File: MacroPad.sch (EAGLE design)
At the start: 16 parts

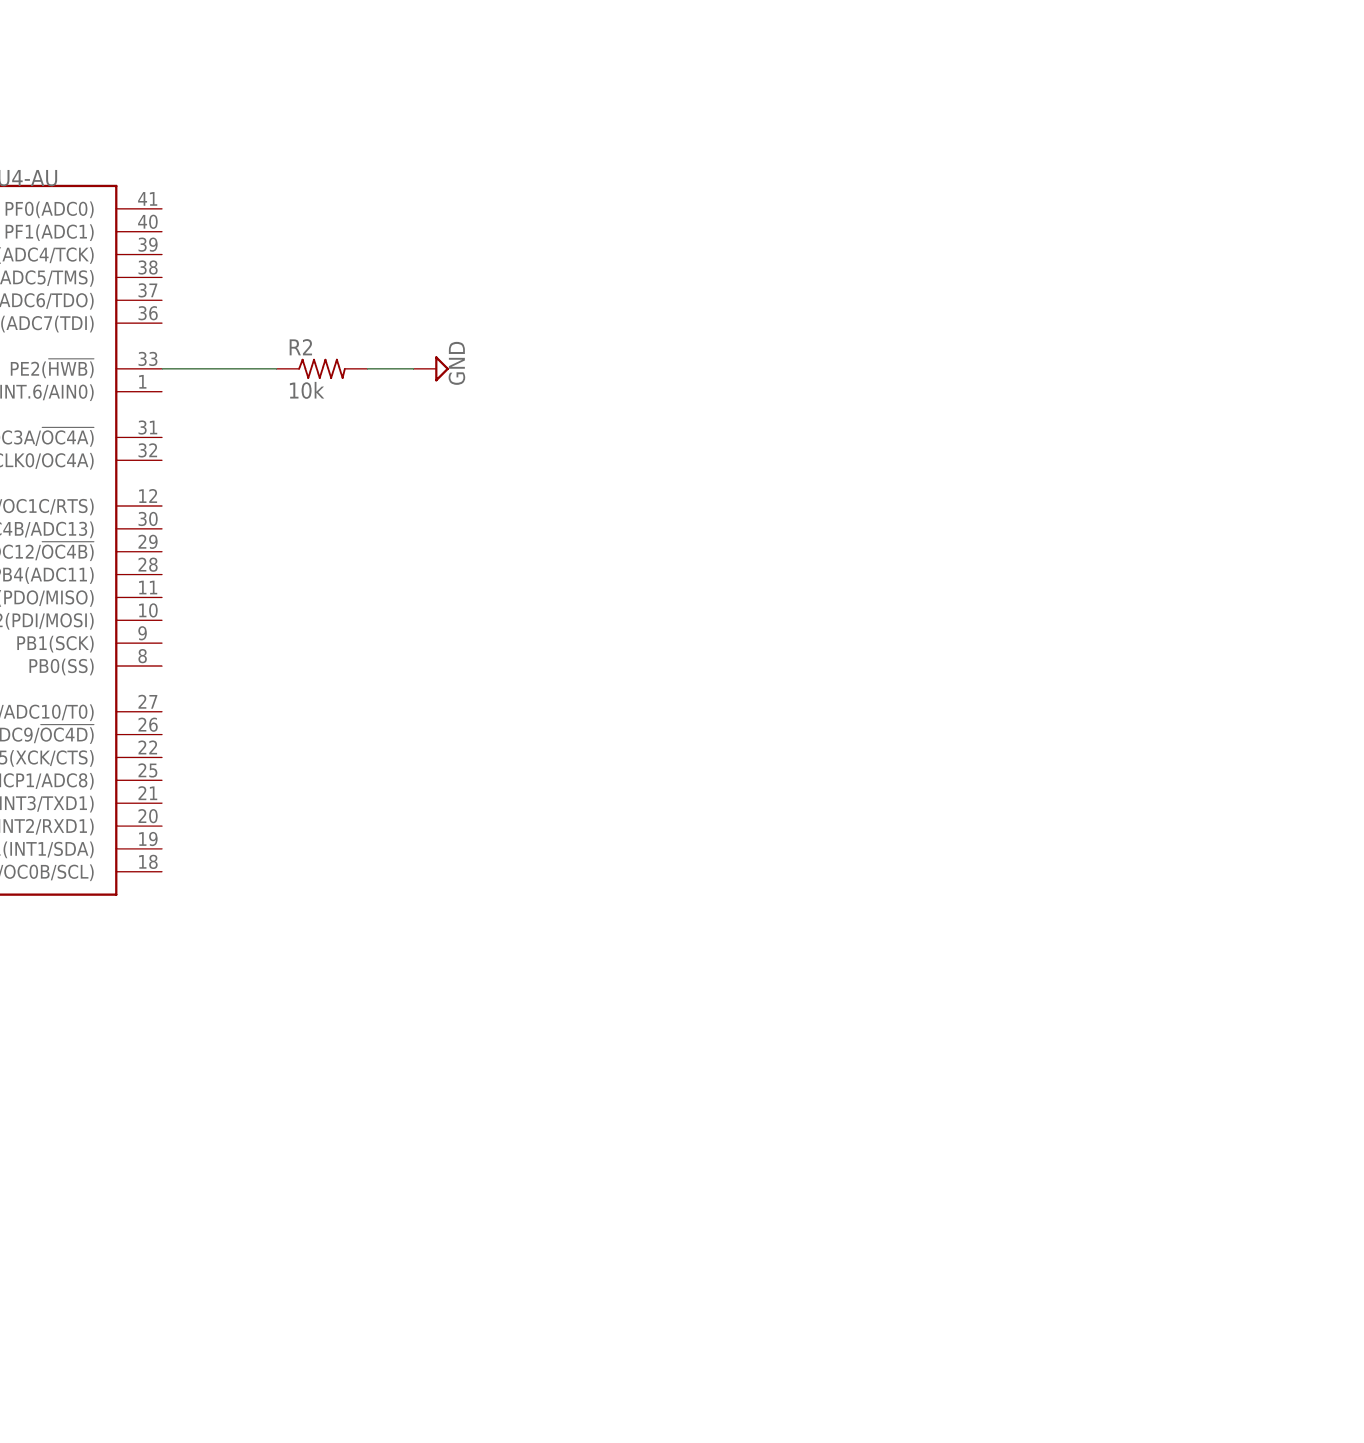
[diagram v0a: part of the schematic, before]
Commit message: Add switch array and connect to microcontroller
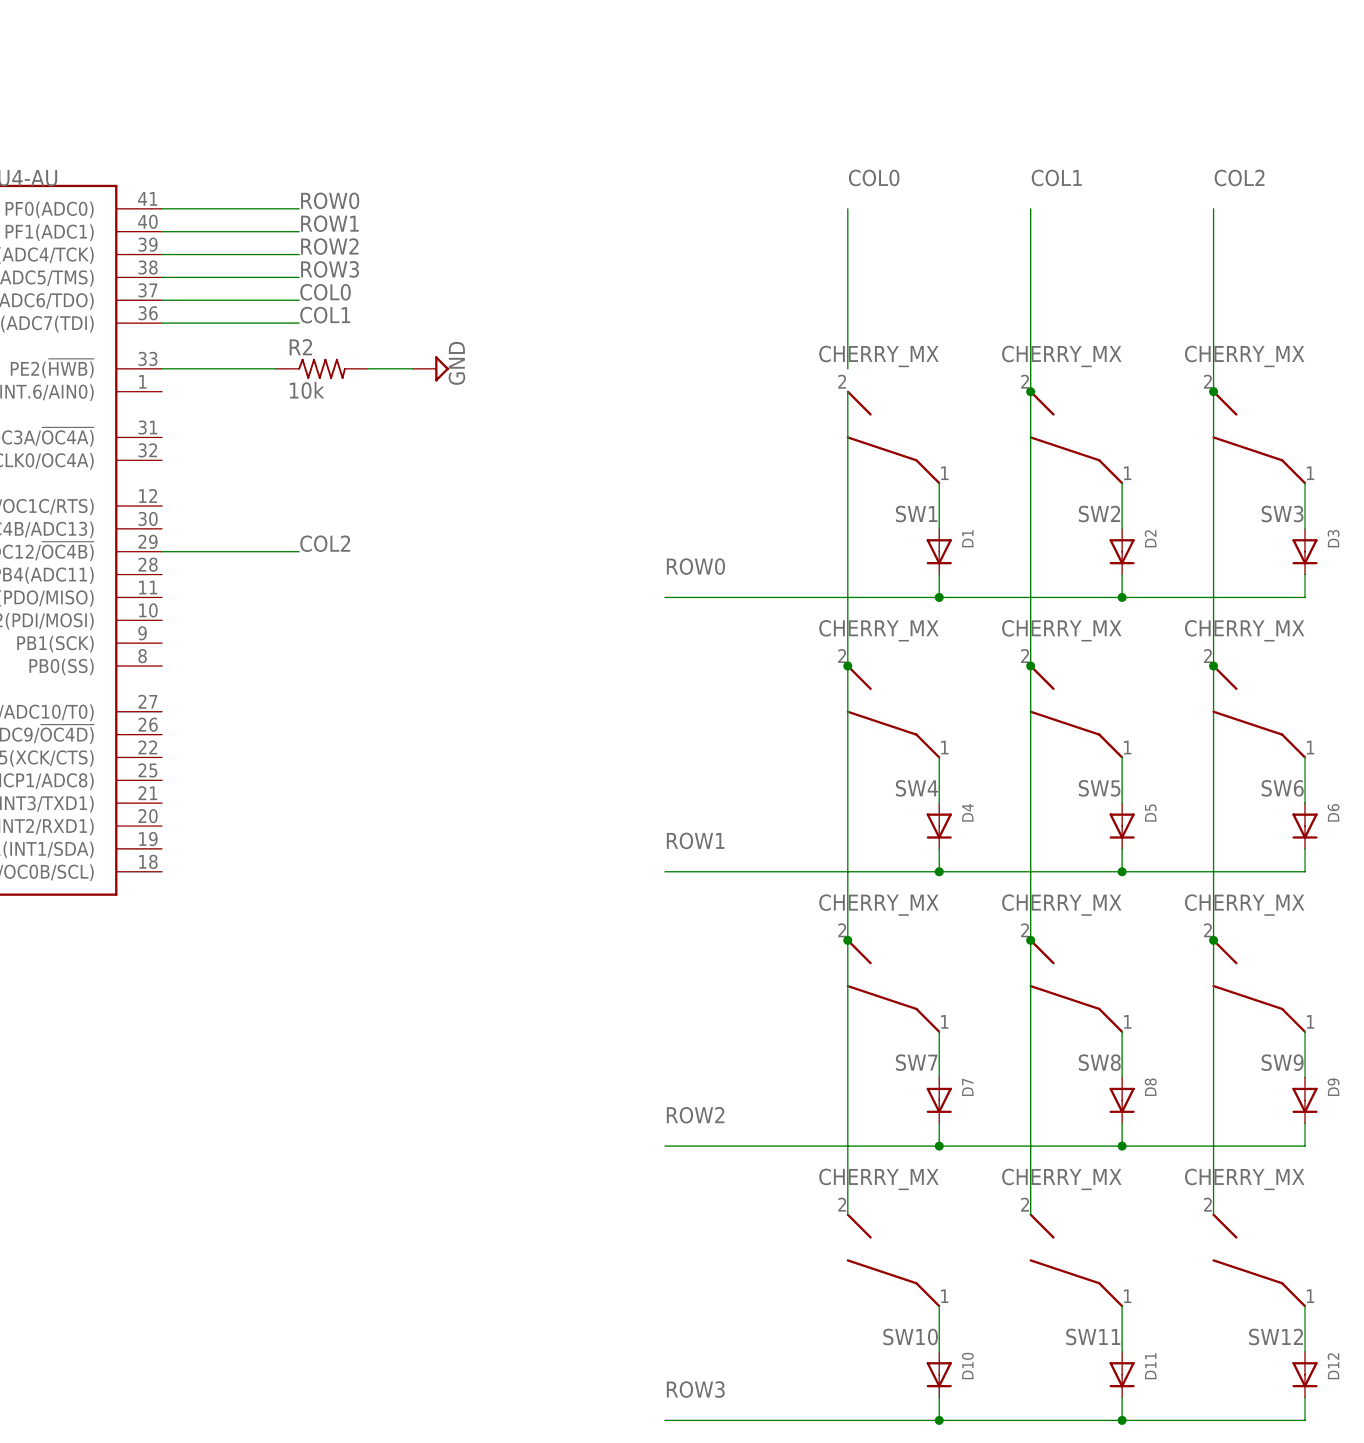
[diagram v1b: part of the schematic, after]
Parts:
- added D1, D10, D11, D12, D2, D3, D4, D5, D6, D7, D8, D9: (no value), adafruit:DIODEDO-1N4148
- added SW1, SW10, SW11, SW12, SW2, SW3, SW4, SW5, SW6, SW7, SW8, SW9: CHERRY_MX, Cherry_MX_v7.0:CHERRY_MX
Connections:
- new net COL0: U$1.PF6(ADC6/TDO)
- new net COL1: SW11.2, SW2.2, SW5.2, SW8.2, U$1.PF7(ADC7(TDI)
- new net COL2: SW12.2, SW3.2, SW6.2, SW9.2, U$1.PB5(OC1A/ADC12/!OC4B)
- new net N$14: D1.A, SW1.1
- new net N$15: D2.A, SW2.1
- new net N$16: D3.A, SW3.1
- new net N$18: SW1.2, SW10.2, SW4.2, SW7.2
- new net N$22: D7.A, SW7.1
- new net N$23: D8.A, SW8.1
- new net N$24: D9.A, SW9.1
- new net N$27: D10.A, SW10.1
- new net N$28: D11.A, SW11.1
- new net N$29: D12.A, SW12.1
- new net N$31: D4.A, SW4.1
- new net N$32: D5.A, SW5.1
- new net N$33: D6.A, SW6.1
- new net ROW0: D1.C, D2.C, D3.C, U$1.PF0(ADC0)
- new net ROW1: D4.C, D5.C, D6.C, U$1.PF1(ADC1)
- new net ROW2: D7.C, D8.C, D9.C, U$1.PF4(ADC4/TCK)
- new net ROW3: D10.C, D11.C, D12.C, U$1.PF5(ADC5/TMS)
